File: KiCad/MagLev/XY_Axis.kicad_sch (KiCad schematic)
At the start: 29 parts, among them Q1 ZX5T851GTA, Q2 ZX5T1951GTA, Q3 ZX5T851GTA, Q4 ZX5T1951GTA, U1 LM324

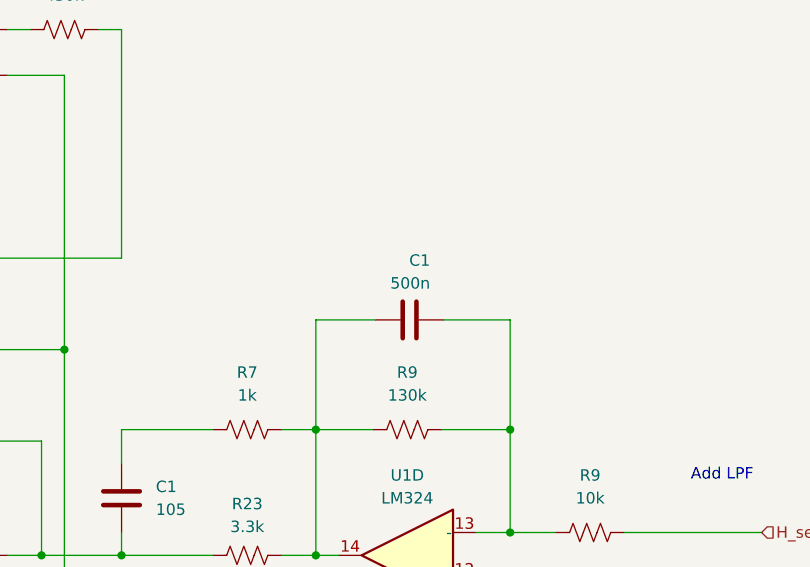
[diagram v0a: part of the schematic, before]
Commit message: Assign footprints to MCU components.
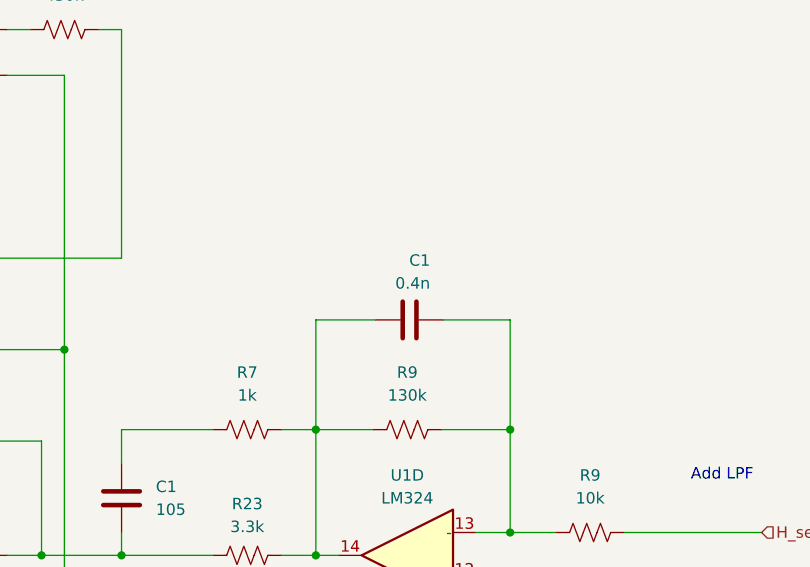
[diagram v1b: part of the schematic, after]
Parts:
- C1: value 500n -> 0.4n
- C2, C3: footprint Capacitor_SMD:CP_Elec_8x10 -> Maglev_Footprint_Library:CP_Elec_8x10_HandSolder
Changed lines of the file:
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@@
       (effects (font (size 1.27 1.27)) (justify left))
     )
-    (property "Footprint" "Capacitor_SMD:CP_Elec_8x10" (at 172.466 142.367 0)
+    (property "Footprint" "Maglev_Footprint_Library:CP_Elec_8x10_HandSolder" (at 172.466 142.367 0)
       (effects (font (size 1.27 1.27)) hide)
     )
@@
       (effects (font (size 1.27 1.27)) (justify left))
     )
-    (property "Value" "500n" (at 195.326 72.136 90)
+    (property "Value" "0.4n" (at 195.326 72.136 90)
       (effects (font (size 1.27 1.27)) (justify left))
     )
@@
       (effects (font (size 1.27 1.27)) (justify left))
     )
-    (property "Footprint" "Capacitor_SMD:CP_Elec_8x10" (at 172.466 129.667 0)
-      (effects (font (size 1.27 1.27)) hide)
-    )
+    (property "Footprint" "Maglev_Footprint_Library:CP_Elec_8x10_HandSolder" (at 172.466 129.667 0)
+      (effects (font (size 1.27 1.27)) hide)
+    )

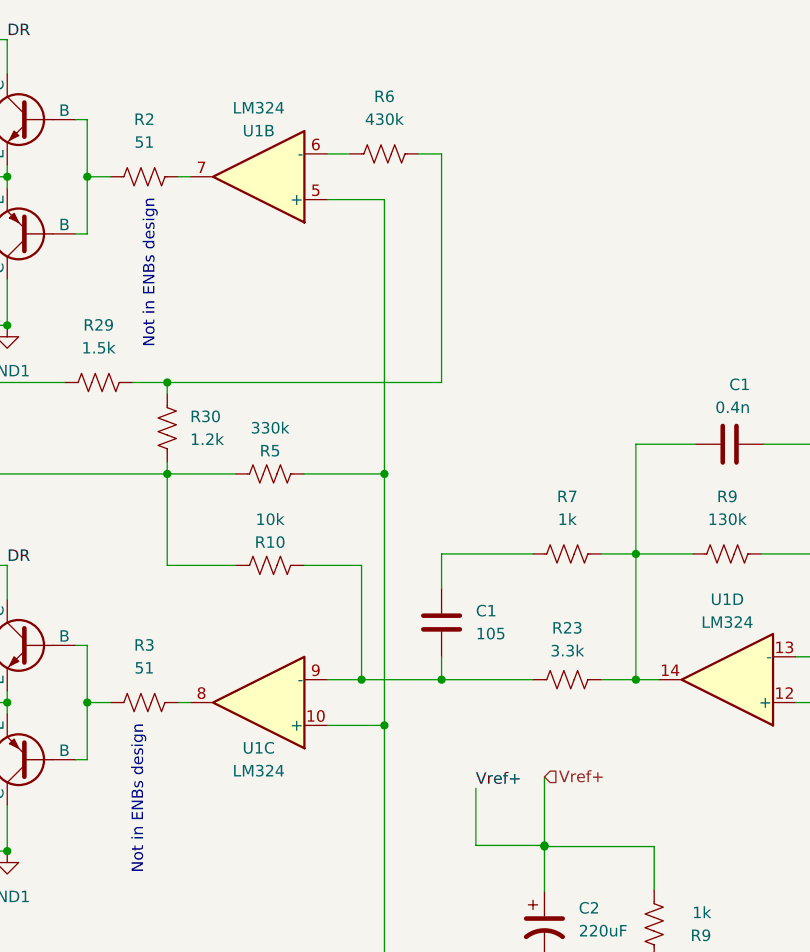
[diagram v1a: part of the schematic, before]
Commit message: Series coils, add TPs.
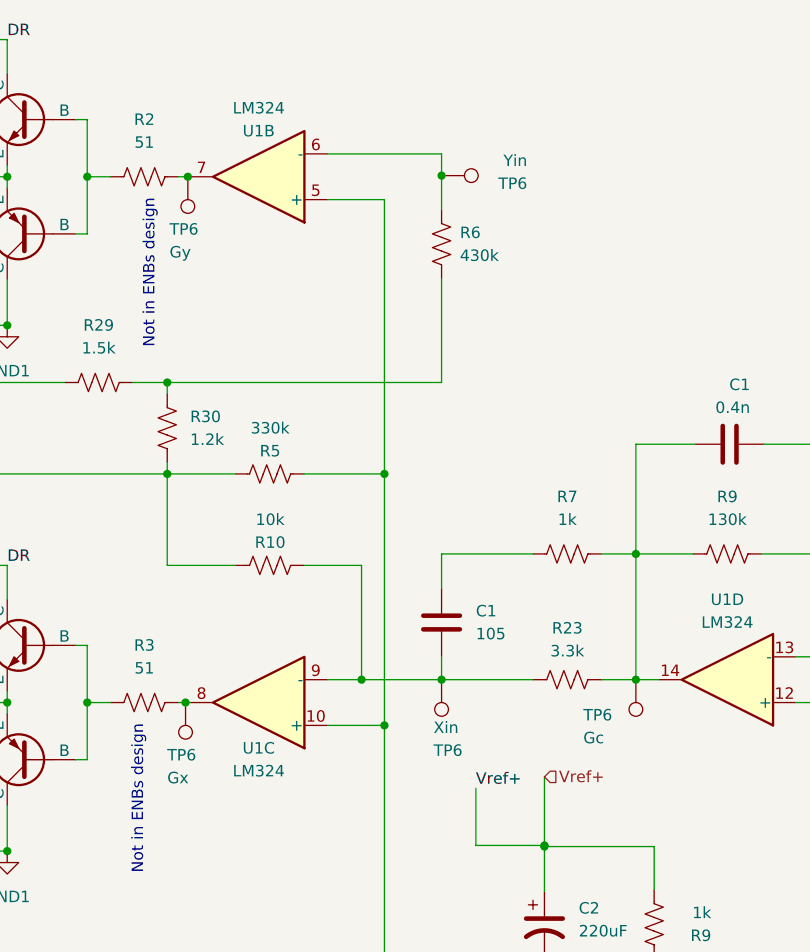
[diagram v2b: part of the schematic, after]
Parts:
- added TP6: Gy, TestPoint:TestPoint_Pad_D2.0mm, symbol Connector:TestPoint
- added TP6: Xin, TestPoint:TestPoint_Pad_D2.0mm, symbol Connector:TestPoint
- added TP6: Gc, TestPoint:TestPoint_Pad_D2.0mm, symbol Connector:TestPoint
- added TP6: Gx, TestPoint:TestPoint_Pad_D2.0mm, symbol Connector:TestPoint
- added TP6: Yin, TestPoint:TestPoint_Pad_D2.0mm, symbol Connector:TestPoint
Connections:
- net at R6.1: now also R29.2, R30.1; no longer U1.6 (-)
- net at C1.2, R10.1, R23.1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: now also TP6.1
- net at C1.1, R23.2, R7.2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: now also TP6.1
- net at R2.2, U1.7: now also TP6.1
- net at R3.2, U1.8: now also TP6.1
- new net: R6.2, TP6.1, U1.6 (-)
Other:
- moved on the sheet: R6
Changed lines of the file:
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@@
   (junction (at 221.996 121.412) (diameter 0) (color 0 0 0 0)
   )
+  (junction (at 161.036 46.355) (diameter 0) (color 0 0 0 0)
+  )
   (junction (at 172.466 147.574) (diameter 0) (color 0 0 0 0)
   )
   (junction (at 112.776 104.902) (diameter 0) (color 0 0 0 0)
   )
+  (junction (at 132.842 46.482) (diameter 0) (color 0 0 0 0)
+  )
   (junction (at 81.026 104.902) (diameter 0) (color 0 0 0 0)
   )
@@
   )
   (junction (at 154.686 79.502) (diameter 0) (color 0 0 0 0)
+  )
+  (junction (at 132.588 104.902) (diameter 0) (color 0 0 0 0)
   )
   (junction (at 172.466 120.904) (diameter 0) (color 0 0 0 0)
@@
   (no_connect (at 49.53 98.044))
   (no_connect (at 49.53 92.964))
-  (wire (pts (xy 148.336 43.942) (xy 150.876 43.942))
+  (wire (pts (xy 148.336 43.942) (xy 161.036 43.942))
     (stroke (width 0) (type default))
   )
@@
     (stroke (width 0) (type default))
   )
-  (wire (pts (xy 133.096 46.482) (xy 131.826 46.482))
+  (wire (pts (xy 133.096 46.482) (xy 132.842 46.482))
     (stroke (width 0) (type default))
   )
@@
     (stroke (width 0) (type default))
   )
-  (wire (pts (xy 161.036 43.942) (xy 158.496 43.942))
-    (stroke (width 0) (type default))
-  )
   (wire (pts (xy 121.666 98.552) (xy 121.666 104.902))
     (stroke (width 0) (type default))
   )
-  (wire (pts (xy 133.096 104.902) (xy 131.826 104.902))
+  (wire (pts (xy 133.096 104.902) (xy 132.588 104.902))
     (stroke (width 0) (type default))
   )
@@
     (stroke (width 0) (type default))
   )
+  (wire (pts (xy 161.036 46.355) (xy 161.036 43.942))
+    (stroke (width 0) (type default))
+  )
   (wire (pts (xy 184.658 145.796) (xy 184.658 147.574))
     (stroke (width 0) (type default))
@@
     (stroke (width 0) (type default))
   )
-  (wire (pts (xy 161.036 69.342) (xy 161.036 43.942))
+  (wire (pts (xy 161.036 69.342) (xy 161.036 57.785))
     (stroke (width 0) (type default))
   )
@@
     (stroke (width 0) (type default))
   )
+  (wire (pts (xy 161.036 50.165) (xy 161.036 46.355))
+    (stroke (width 0) (type default))
+  )
   (wire (pts (xy 184.658 125.73) (xy 184.658 120.904))
     (stroke (width 0) (type default))
   )
+  (wire (pts (xy 132.588 104.902) (xy 131.826 104.902))
+    (stroke (width 0) (type default))
+  )
   (wire (pts (xy 161.036 88.392) (xy 171.196 88.392))
     (stroke (width 0) (type default))
@@
   )
   (wire (pts (xy 112.776 93.472) (xy 112.776 89.662))
+    (stroke (width 0) (type default))
+  )
+  (wire (pts (xy 132.842 46.482) (xy 131.826 46.482))
     (stroke (width 0) (type default))
   )
@@
     )
   )
-  (symbol (lib_id "Device:R_US") (at 154.686 43.942 90) (unit 1)
+  (symbol (lib_id "Device:R_US") (at 161.036 53.975 180) (unit 1)
     (in_bom yes) (on_board yes) (dnp no) (fields_autoplaced)
-    (property "Reference" "R6" (at 154.686 37.592 90)
-      (effects (font (size 1.27 1.27)))
-    )
-    (property "Value" "430k" (at 154.686 40.132 90)
-      (effects (font (size 1.27 1.27)))
-    )
-    (property "Footprint" "Resistor_SMD:R_0805_2012Metric_Pad1.20x1.40mm_HandSolder" (at 154.94 42.926 90)
-      (effects (font (size 1.27 1.27)) hide)
-    )
-    (property "Datasheet" "~" (at 154.686 43.942 0)
+    (property "Reference" "R6" (at 163.068 52.705 0)
+      (effects (font (size 1.27 1.27)) (justify right))
+    )
+    (property "Value" "430k" (at 163.068 55.245 0)
+      (effects (font (size 1.27 1.27)) (justify right))
+    )
+    (property "Footprint" "Resistor_SMD:R_0805_2012Metric_Pad1.20x1.40mm_HandSolder" (at 160.02 53.721 90)
+      (effects (font (size 1.27 1.27)) hide)
+    )
+    (property "Datasheet" "~" (at 161.036 53.975 0)
       (effects (font (size 1.27 1.27)) hide)
     )
@@
     )
   )
+  (symbol (lib_id "Connector:TestPoint") (at 132.842 46.482 180) (unit 1)
+    (in_bom yes) (on_board yes) (dnp no)
+    (property "Reference" "TP6" (at 130.81 52.324 0)
+      (effects (font (size 1.27 1.27)) (justify right))
+    )
+    (property "Value" "Gy" (at 130.81 54.864 0)
+      (effects (font (size 1.27 1.27)) (justify right))
+    )
+    (property "Footprint" "TestPoint:TestPoint_Pad_D2.0mm" (at 127.762 46.482 0)
+      (effects (font (size 1.27 1.27)) hide)
+    )
+    (property "Datasheet" "~" (at 127.762 46.482 0)
+      (effects (font (size 1.27 1.27)) hide)
+    )
+    (pin "1")
+    (instances
+      (project "MagLev"
+        (path "/5eab7e8b-54e1-47d0-9dc3-1e7c3fa2f560"
+          (reference "TP6") (unit 1)
+        )
+        (path "/5eab7e8b-54e1-47d0-9dc3-1e7c3fa2f560/1b1a7f40-4880-4dc8-87d1-1ed1d4fb8d1e"
+          (reference "TP15") (unit 1)
+        )
+        (path "/5eab7e8b-54e1-47d0-9dc3-1e7c3fa2f560/7df46fb0-abf8-474a-ba30-7ff9455482b6"
+          (reference "TP16") (unit 1)
+        )
+      )
+    )
+  )
   (symbol (lib_id "power:GND") (at 38.608 74.422 0) (unit 1)
     (in_bom yes) (on_board yes) (dnp no) (fields_autoplaced)
@@
         (path "/5eab7e8b-54e1-47d0-9dc3-1e7c3fa2f560/7df46fb0-abf8-474a-ba30-7ff9455482b6"
           (reference "#PWR06") (unit 1)
+        )
+      )
+    )
+  )
+  (symbol (lib_id "Connector:TestPoint") (at 161.036 102.362 180) (unit 1)
+    (in_bom yes) (on_board yes) (dnp no)
+    (property "Reference" "TP6" (at 160.147 110.236 0)
+      (effects (font (size 1.27 1.27)) (justify right))
+    )
+    (property "Value" "Xin" (at 160.147 107.696 0)
+      (effects (font (size 1.27 1.27)) (justify right))
+    )
+    (property "Footprint" "TestPoint:TestPoint_Pad_D2.0mm" (at 155.956 102.362 0)
+      (effects (font (size 1.27 1.27)) hide)
+    )
+    (property "Datasheet" "~" (at 155.956 102.362 0)
+      (effects (font (size 1.27 1.27)) hide)
+    )
+    (pin "1")
+    (instances
+      (project "MagLev"
+        (path "/5eab7e8b-54e1-47d0-9dc3-1e7c3fa2f560"
+          (reference "TP6") (unit 1)
+        )
+        (path "/5eab7e8b-54e1-47d0-9dc3-1e7c3fa2f560/1b1a7f40-4880-4dc8-87d1-1ed1d4fb8d1e"
+          (reference "TP22") (unit 1)
+        )
+        (path "/5eab7e8b-54e1-47d0-9dc3-1e7c3fa2f560/7df46fb0-abf8-474a-ba30-7ff9455482b6"
+          (reference "TP23") (unit 1)
+        )
+      )
+    )
+  )
+  (symbol (lib_id "Connector:TestPoint") (at 182.626 102.362 180) (unit 1)
+    (in_bom yes) (on_board yes) (dnp no)
+    (property "Reference" "TP6" (at 176.784 106.299 0)
+      (effects (font (size 1.27 1.27)) (justify right))
+    )
+    (property "Value" "Gc" (at 176.784 108.839 0)
+      (effects (font (size 1.27 1.27)) (justify right))
+    )
+    (property "Footprint" "TestPoint:TestPoint_Pad_D2.0mm" (at 177.546 102.362 0)
+      (effects (font (size 1.27 1.27)) hide)
+    )
+    (property "Datasheet" "~" (at 177.546 102.362 0)
+      (effects (font (size 1.27 1.27)) hide)
+    )
+    (pin "1")
+    (instances
+      (project "MagLev"
+        (path "/5eab7e8b-54e1-47d0-9dc3-1e7c3fa2f560"
+          (reference "TP6") (unit 1)
+        )
+        (path "/5eab7e8b-54e1-47d0-9dc3-1e7c3fa2f560/1b1a7f40-4880-4dc8-87d1-1ed1d4fb8d1e"
+          (reference "TP11") (unit 1)
+        )
+        (path "/5eab7e8b-54e1-47d0-9dc3-1e7c3fa2f560/7df46fb0-abf8-474a-ba30-7ff9455482b6"
+          (reference "TP12") (unit 1)
         )
       )
@@
     )
   )
+  (symbol (lib_id "Connector:TestPoint") (at 132.588 104.902 180) (unit 1)
+    (in_bom yes) (on_board yes) (dnp no)
+    (property "Reference" "TP6" (at 130.556 110.744 0)
+      (effects (font (size 1.27 1.27)) (justify right))
+    )
+    (property "Value" "Gx" (at 130.556 113.284 0)
+      (effects (font (size 1.27 1.27)) (justify right))
+    )
+    (property "Footprint" "TestPoint:TestPoint_Pad_D2.0mm" (at 127.508 104.902 0)
+      (effects (font (size 1.27 1.27)) hide)
+    )
+    (property "Datasheet" "~" (at 127.508 104.902 0)
+      (effects (font (size 1.27 1.27)) hide)
+    )
+    (pin "1")
+    (instances
+      (project "MagLev"
+        (path "/5eab7e8b-54e1-47d0-9dc3-1e7c3fa2f560"
+          (reference "TP6") (unit 1)
+        )
+        (path "/5eab7e8b-54e1-47d0-9dc3-1e7c3fa2f560/1b1a7f40-4880-4dc8-87d1-1ed1d4fb8d1e"
+          (reference "TP13") (unit 1)
+        )
+        (path "/5eab7e8b-54e1-47d0-9dc3-1e7c3fa2f560/7df46fb0-abf8-474a-ba30-7ff9455482b6"
+          (reference "TP14") (unit 1)
+        )
+      )
+    )
+  )
   (symbol (lib_id "Device:R_US") (at 141.986 79.502 270) (unit 1)
     (in_bom yes) (on_board yes) (dnp no)
@@
         )
       )
+    )
+  )
+  (symbol (lib_id "Connector:TestPoint") (at 161.036 46.355 270) (unit 1)
+    (in_bom yes) (on_board yes) (dnp no)
+    (property "Reference" "TP6" (at 170.561 47.244 90)
+      (effects (font (size 1.27 1.27)) (justify right))
+    )
+    (property "Value" "Yin" (at 170.561 44.704 90)
+      (effects (font (size 1.27 1.27)) (justify right))
+    )
+    (property "Footprint" "TestPoint:TestPoint_Pad_D2.0mm" (at 161.036 51.435 0)
+      (effects (font (size 1.27 1.27)) hide)
+    )
+    (property "Datasheet" "~" (at 161.036 51.435 0)
+      (effects (font (size 1.27 1.27)) hide)
+    )
+    (pin "1")
+    (instances
+      (project "MagLev"
+        (path "/5eab7e8b-54e1-47d0-9dc3-1e7c3fa2f560"
+          (reference "TP6") (unit 1)
+        )
+        (path "/5eab7e8b-54e1-47d0-9dc3-1e7c3fa2f560/1b1a7f40-4880-4dc8-87d1-1ed1d4fb8d1e"
+          (reference "TP20") (unit 1)
+        )
+        (path "/5eab7e8b-54e1-47d0-9dc3-1e7c3fa2f560/7df46fb0-abf8-474a-ba30-7ff9455482b6"
+          (reference "TP21") (unit 1)
+        )
+      )

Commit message: Add netclasses, define PCB rules.
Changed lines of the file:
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@@
-    (stroke (width 0) (type default))
-  )
-  (wire (pts (xy 112.776 31.242) (xy 93.726 31.242))
     (stroke (width 0) (type default))
   )
@@
   )
   (wire (pts (xy 112.776 93.472) (xy 112.776 89.662))
+    (stroke (width 0) (type default))
+  )
+  (wire (pts (xy 93.726 31.242) (xy 112.776 31.242))
     (stroke (width 0) (type default))
   )
@@
     (effects (font (size 1.27 1.27)) (justify right))
   )
+  (netclass_flag "" (length 2.54) (shape round) (at 96.52 31.242 0) (fields_autoplaced)
+    (effects (font (size 1.27 1.27)) (justify left bottom))
+    (property "Netclass" "HighCurrent" (at 97.2185 28.702 0)
+      (effects (font (size 1.27 1.27) italic) (justify left))
+    )
+  )
+  (netclass_flag "" (length 2.54) (shape round) (at 100.965 79.502 0) (fields_autoplaced)
+    (effects (font (size 1.27 1.27)) (justify left bottom))
+    (property "Netclass" "HighCurrent" (at 101.6635 76.962 0)
+      (effects (font (size 1.27 1.27) italic) (justify left))
+    )
+  )
+  (netclass_flag "" (length 2.54) (shape round) (at 95.758 62.992 0) (fields_autoplaced)
+    (effects (font (size 1.27 1.27)) (justify left bottom))
+    (property "Netclass" "HighCurrent" (at 96.4565 60.452 0)
+      (effects (font (size 1.27 1.27) italic) (justify left))
+    )
+  )
+  (netclass_flag "" (length 2.54) (shape round) (at 91.821 69.342 0) (fields_autoplaced)
+    (effects (font (size 1.27 1.27)) (justify left bottom))
+    (property "Netclass" "HighCurrent" (at 92.5195 66.802 0)
+      (effects (font (size 1.27 1.27) italic) (justify left))
+    )
+  )
+  (netclass_flag "" (length 2.54) (shape round) (at 95.25 89.662 0) (fields_autoplaced)
+    (effects (font (size 1.27 1.27)) (justify left bottom))
+    (property "Netclass" "HighCurrent" (at 95.9485 87.122 0)
+      (effects (font (size 1.27 1.27) italic) (justify left))
+    )
+  )
+  (netclass_flag "" (length 2.54) (shape round) (at 96.647 121.412 0) (fields_autoplaced)
+    (effects (font (size 1.27 1.27)) (justify left bottom))
+    (property "Netclass" "HighCurrent" (at 97.3455 118.872 0)
+      (effects (font (size 1.27 1.27) italic) (justify left))
+    )
+  )
   (symbol (lib_id "Simulation_SPICE:PNP") (at 115.316 111.252 180) (unit 1)

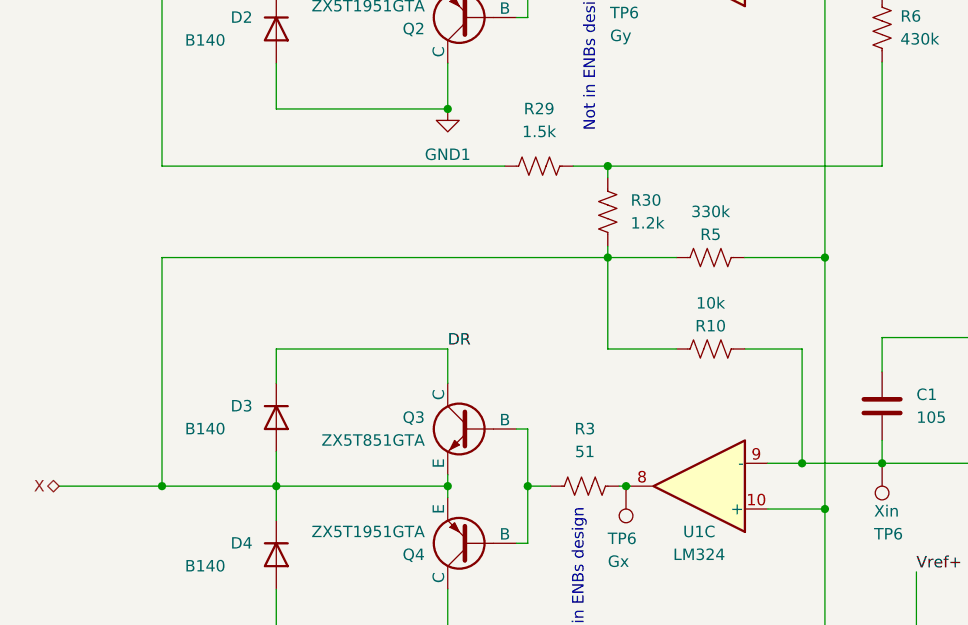
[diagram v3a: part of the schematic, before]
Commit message: Place and route MCU page components.
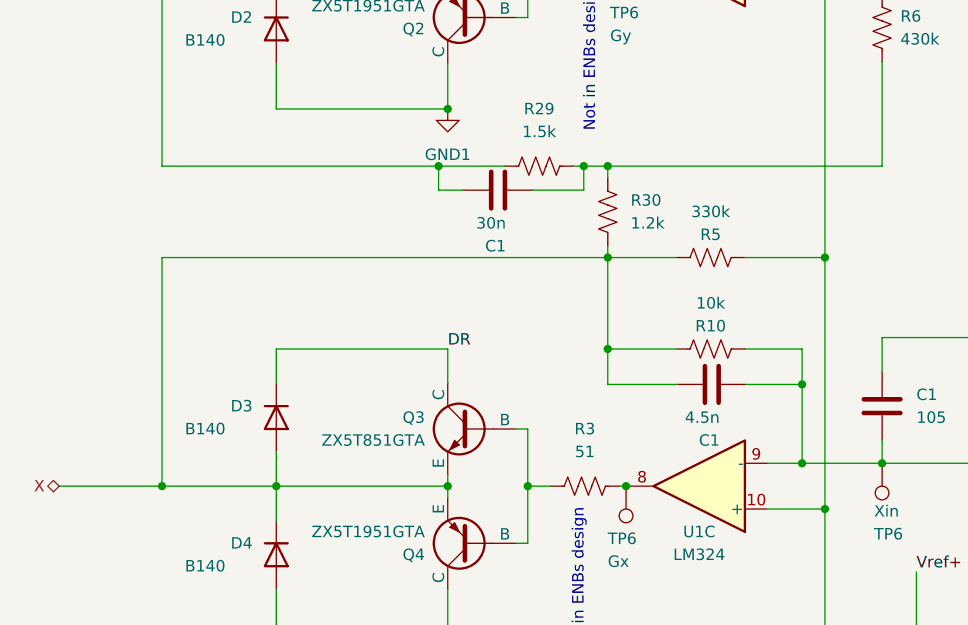
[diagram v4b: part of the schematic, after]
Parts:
- added C1: 30n, Capacitor_SMD:C_0805_2012Metric_Pad1.18x1.45mm_HandSolder, symbol Device:C
- added C1: 4.5n, Capacitor_SMD:C_0805_2012Metric_Pad1.18x1.45mm_HandSolder, symbol Device:C
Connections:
- net X: now also C1.1
- net Y: now also C1.1
- net at R29.2, R30.1, R6.1: now also C1.2
- net at C1.2, R10.1, R23.1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: now also C1.2
